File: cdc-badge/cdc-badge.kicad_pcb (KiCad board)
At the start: 4 copper layers, 85 x 110 mm, 158 parts, among them J1 USB_C, J2 JST S2B-PH-SM4-TB, J3 Conn_02x20_Odd_Even, J4 Conn_Grove, J5 Conn_02x03_Odd_Even, J6 Conn_01x06, J7 Conn_01x24, Q1 Si1308EDL, Q2 Si1308EDL, SW0 0, SW1 1, SW10 YES, SW11 NO, SW12 power on/reset, SW13 reset, SW14 flash/power off, SW15 MST-22D18G2 3J, SW16 MST-22D18G2 3J, SW2 2, SW3 3, SW4 4, SW5 5, SW6 6, SW7 7, SW8 8, SW9 9, U1 ESP32-S3-WROOM-1-N16R8, U2 TCA9535PWR, U3 TR01-C2P-T301, U5 TLV61070ADBVR, U6 BQ25895RTW, U8 TLV62569DBV

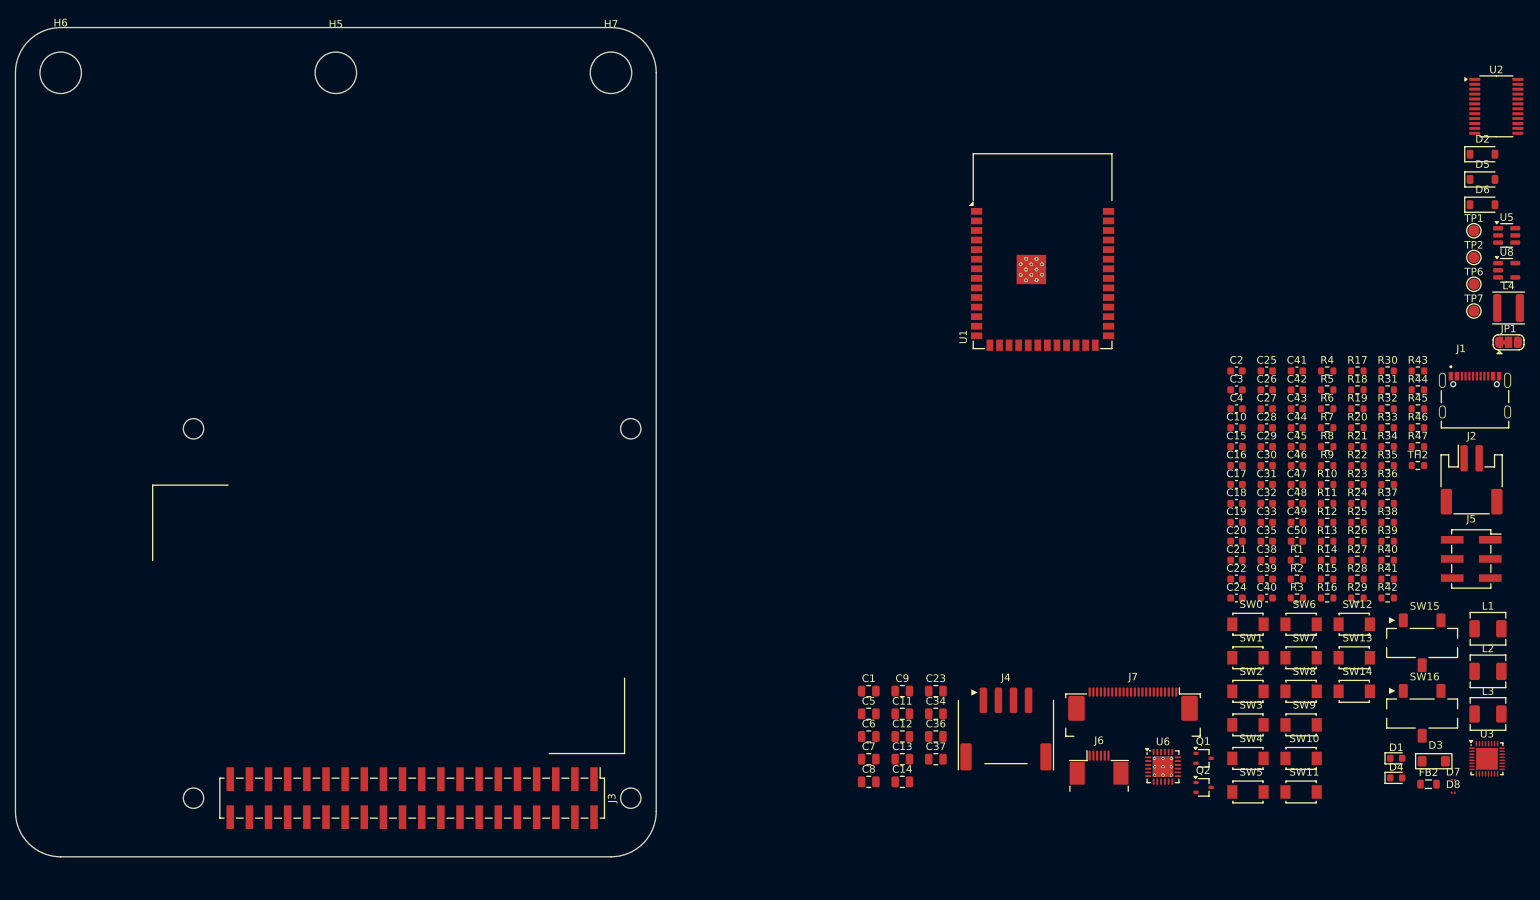
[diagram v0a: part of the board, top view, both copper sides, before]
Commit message: PCB: Placing the connectors, display and battery and lock them
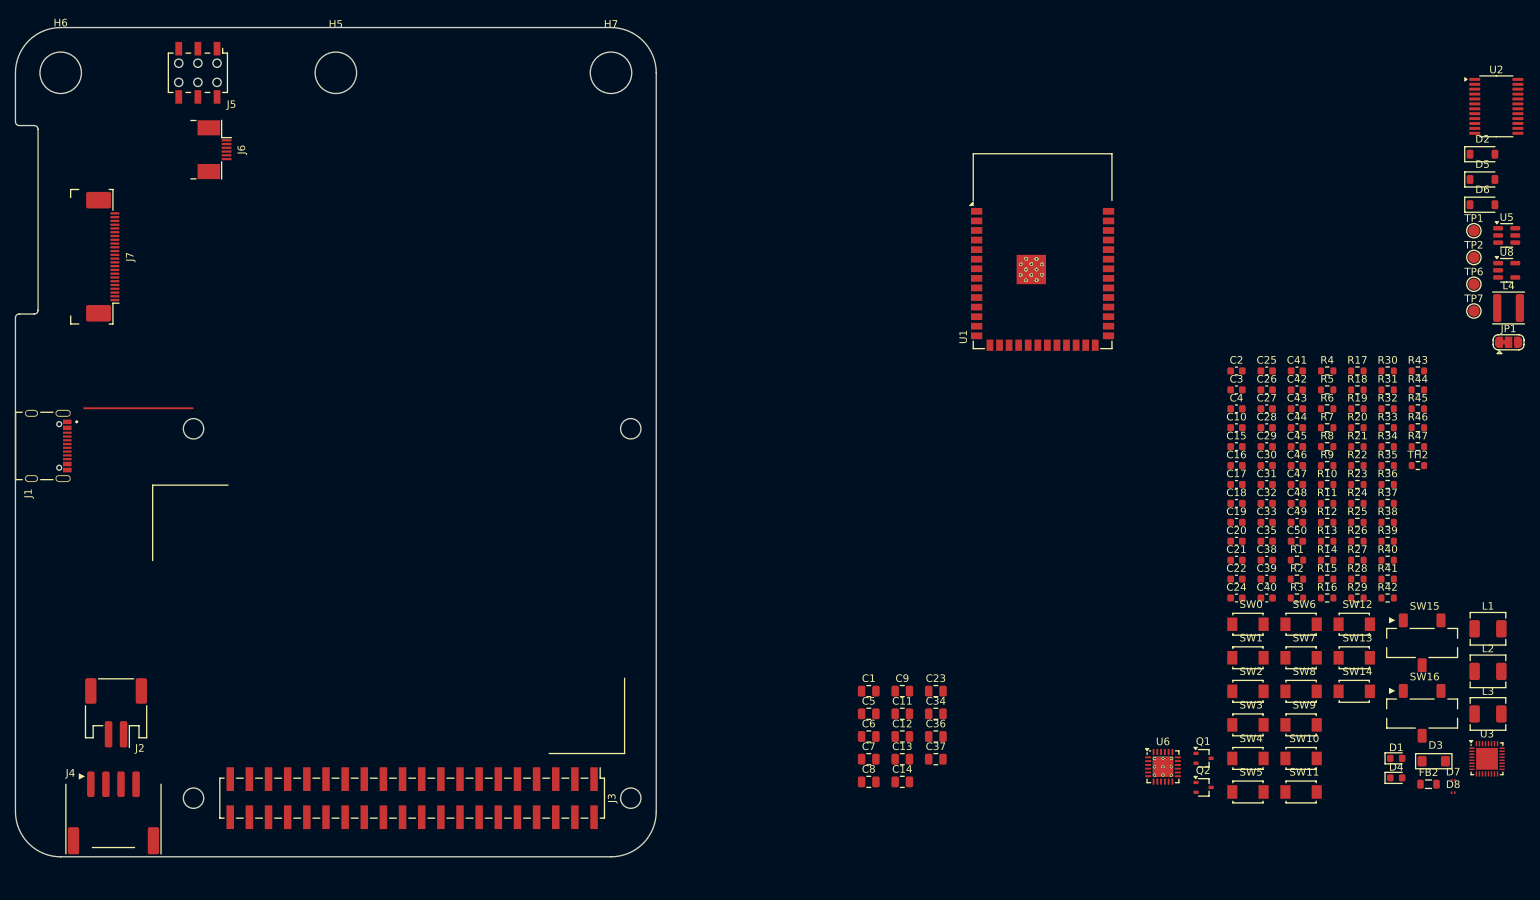
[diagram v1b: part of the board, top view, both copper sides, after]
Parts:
- J5: footprint Connector_PinSocket_2.54mm:PinSocket_2x03_P2.54mm_Vertical_SMD -> Connector_Wuerth:Wuerth_WR-PHD_610006243021_SMD_2x03_P2.54mm_Vertical
- moved J1 190.5 mm to (58.2, 104.5), turned to -90 degrees
- moved J2 182.4 mm to (68.3, 139.9), turned to 180 degrees
- moved J5 180.8 mm to (79.2, 55.0), turned to -90 degrees
- moved J7 149.8 mm to (66.0, 79.4), turned to -90 degrees
- moved J6 143.1 mm to (81.4, 65.2), turned to -90 degrees
- moved J4 118.9 mm to (68.0, 154.0)
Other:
- outline, holes or cut-outs redrawn

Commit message: PCB: Sort the components to their corresponding role/areas
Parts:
- moved D8 216.4 mm to (44.8, 70.0)
- moved D7 214.6 mm to (45.0, 73.0)
- moved FB2 209.0 mm to (44.9, 81.0)
- moved D3 206.4 mm to (44.5, 90.0)
- moved R1 180.8 mm to (45.0, 103.0)
- moved R2 180.6 mm to (44.8, 110.0)
- moved Q1 133.7 mm to (275.0, 27.6)
- moved C34 128.8 mm to (253.0, 36.0)
- moved D4 127.7 mm to (169.2, 41.0)
- moved C23 117.8 mm to (236.1, 35.0)
- moved Q2 109.3 mm to (240.0, 44.0)
- moved L1 100.2 mm to (162.8, 80.0)
- moved JP1 100.1 mm to (182.7, 162.0)
- moved C24 98.6 mm to (260.0, 36.0)
- moved D1 95.7 mm to (162.8, 87.0)
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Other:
- board text added: "3V"
- board text added: "5V"
- board text added: "Btn"
- board text added: "Charger"
- board text added: "Epaper"
- board text added: "Expander"
- board text added: "TR"

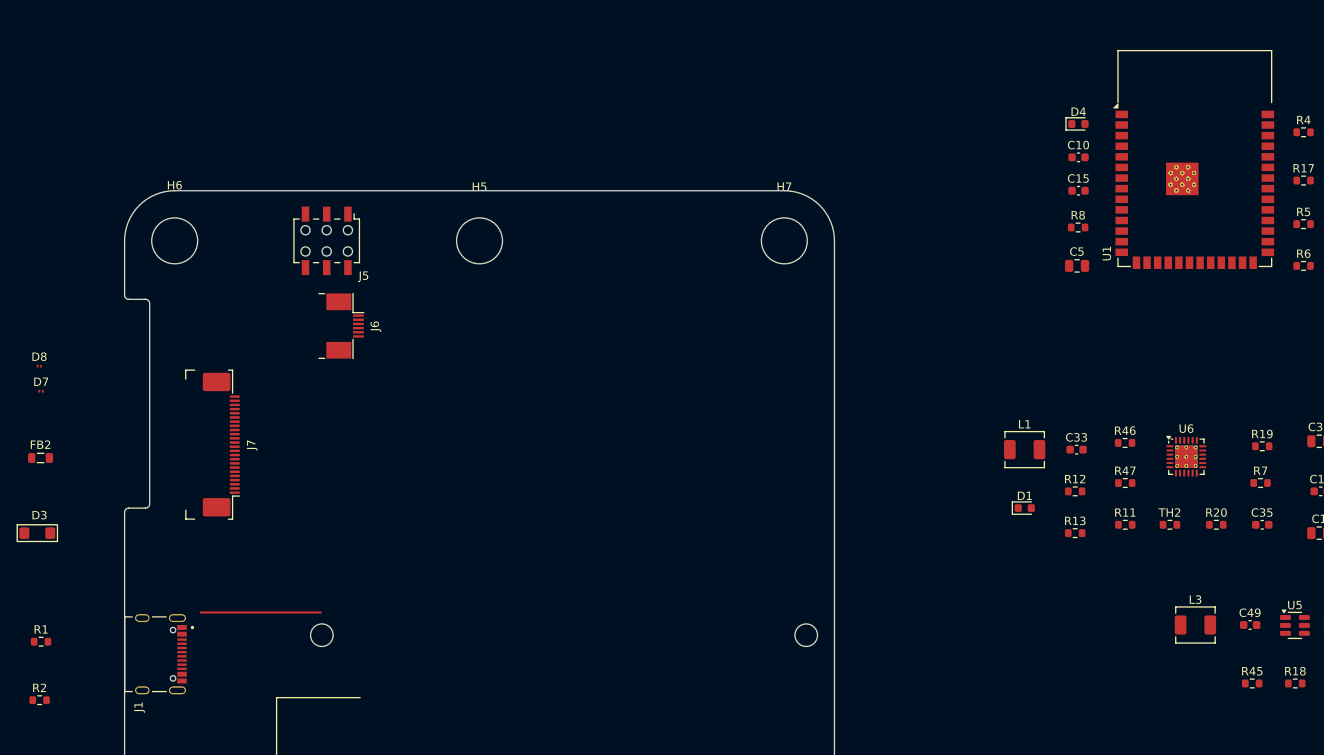
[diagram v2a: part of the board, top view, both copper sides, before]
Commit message: PCB: USB-C, Datatracks and Charging IC placement draft
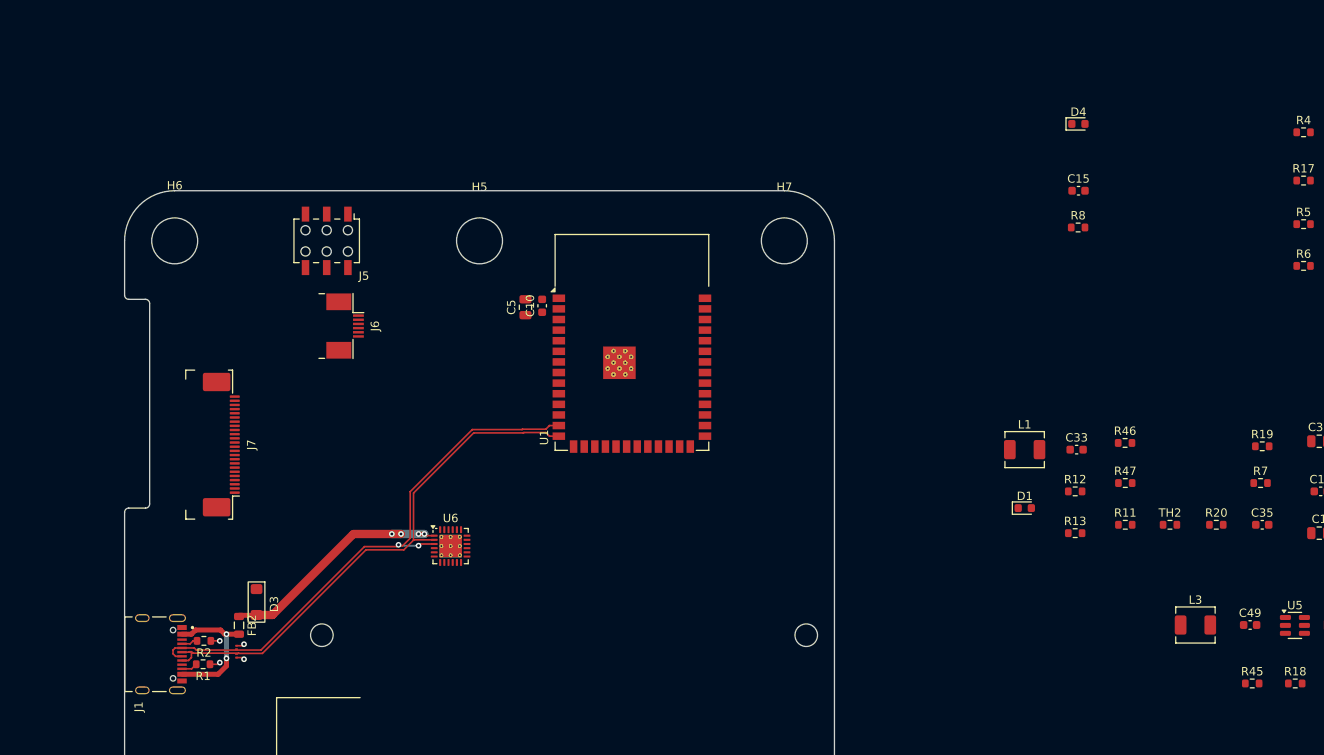
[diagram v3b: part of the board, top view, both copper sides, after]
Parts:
- moved U6 88.7 mm to (94.0, 91.5)
- moved U1 70.9 mm to (115.8, 67.1)
- moved C10 66.6 mm to (105.0, 62.8), turned to 90 degrees
- moved C5 66.2 mm to (103.0, 63.0), turned to 90 degrees
- moved D8 42.0 mm to (68.4, 104.7), turned to -90 degrees
- moved D7 38.6 mm to (68.4, 103.7), turned to 90 degrees
- moved FB2 31.1 mm to (68.7, 101.0), turned to -90 degrees
- moved D3 27.5 mm to (70.8, 98.2), turned to -90 degrees
- moved R2 20.9 mm to (64.5, 102.9), turned to 180 degrees
- moved R1 19.6 mm to (64.4, 105.7), turned to 180 degrees
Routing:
- net /USB_D-: track 0.00 -> 66.9 mm, vias 0 -> 2
- net /USB_D+: track 0.00 -> 64.1 mm
- net VBUS: track 0.00 -> 29.1 mm, vias 0 -> 4
- net /PRE_VBUS: track 0.00 -> 16.8 mm, vias 0 -> 2
- net GND: track 0.00 -> 4.29 mm, vias 0 -> 4
- net Net-(J1-CC1): track 0.00 -> 1.94 mm
- net Net-(J1-CC2): track 0.00 -> 1.93 mm

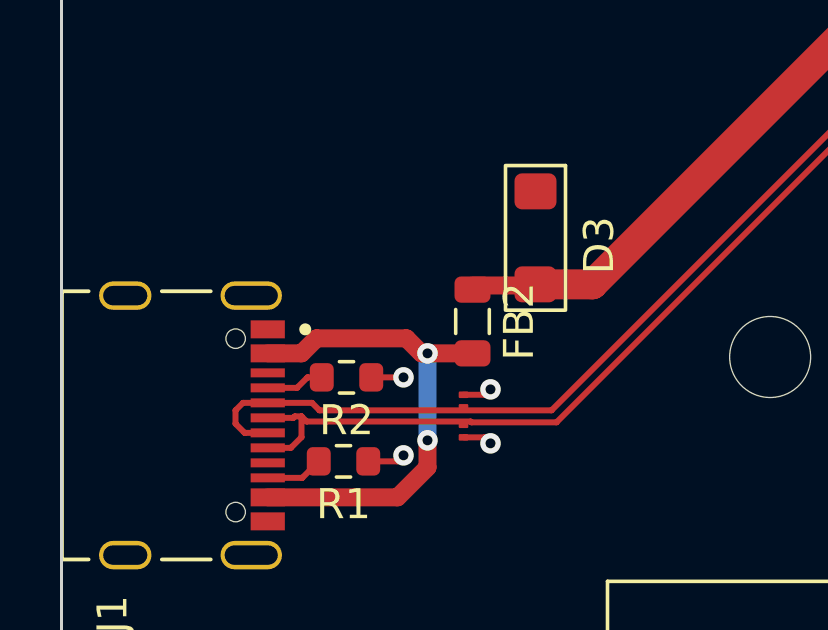
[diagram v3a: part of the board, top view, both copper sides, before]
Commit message: pcb: set default widths and clearances, try copper pours
Defaults set for both tracks and vias.
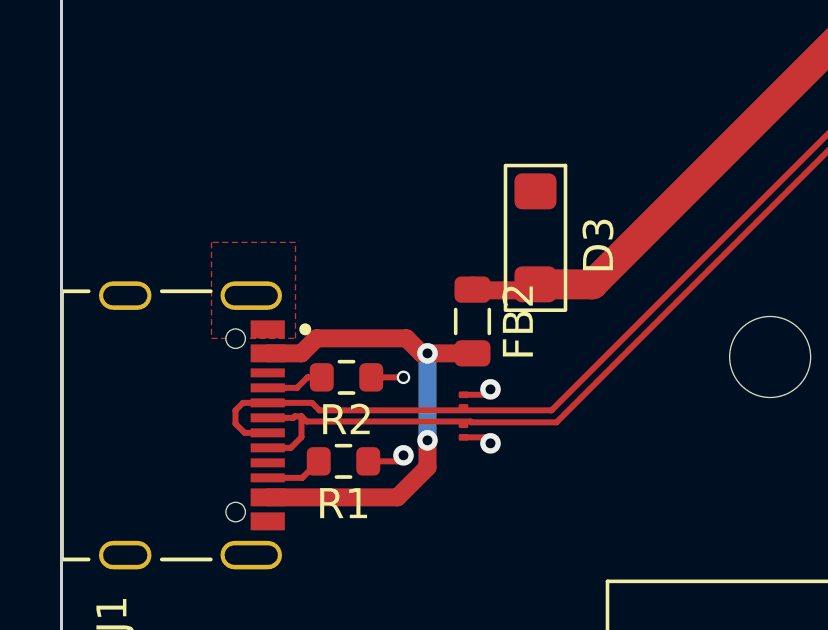
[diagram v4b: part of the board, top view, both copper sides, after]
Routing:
- added copper zone on F.Cu, net GND
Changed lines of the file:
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@@
 		(0 "F.Cu" signal)
 		(4 "In1.Cu" power "In1.Cu.GND")
-		(6 "In2.Cu" power "In2.Cu.VCC")
+		(6 "In2.Cu" power "In2.Cu.GND")
 		(2 "B.Cu" signal)
 		(9 "F.Adhes" user "F.Adhesive")
@@
 	)
 	(via
-		(at 69.3 105.1)
-		(size 0.6858)
-		(drill 0.3302)
+		(at 66.4 102.9)
+		(size 0.45)
+		(drill 0.3)
 		(layers "F.Cu" "B.Cu")
 		(net 1)
 	)
 	(via
-		(at 66.4 105.5)
+		(at 69.3 105.1)
 		(size 0.6858)
 		(drill 0.3302)
@@
 	)
 	(via
-		(at 66.4 102.9)
+		(at 66.4 105.5)
 		(size 0.6858)
 		(drill 0.3302)
@@
 	)
 	(segment
-		(start 70.7625 99.8375)
-		(end 70.8 99.8)
-		(width 0.6)
-		(layer "F.Cu")
-		(net 55)
-	)
-	(segment
-		(start 68.7 99.8375)
-		(end 70.7625 99.8375)
-		(width 0.6)
-		(layer "F.Cu")
-		(net 55)
-	)
-	(segment
 		(start 72.7 99.8)
 		(end 82.3 90.2)
@@
 	)
 	(segment
+		(start 70.6 100)
+		(end 70.8 99.8)
+		(width 0.6)
+		(layer "F.Cu")
+		(net 55)
+	)
+	(segment
 		(start 91.1 90.3)
 		(end 90.9 90.1)
@@
 		(net 55)
 	)
+	(segment
+		(start 68.8625 100)
+		(end 70.6 100)
+		(width 0.6)
+		(layer "F.Cu")
+		(net 55)
+	)
+	(segment
+		(start 68.7 99.8375)
+		(end 68.8625 100)
+		(width 0.6)
+		(layer "F.Cu")
+		(net 55)
+	)
 	(via
 		(at 87 90.1)
@@
 		(net 75)
 	)
+	(zone
+		(net 1)
+		(net_name "GND")
+		(layer "F.Cu")
+		(hatch edge 0.5)
+		(connect_pads yes
+			(clearance 0.2)
+		)
+		(min_thickness 0.2)
+		(filled_areas_thickness no)
+		(fill yes
+			(thermal_gap 0.5)
+			(thermal_bridge_width 0.5)
+		)
+		(polygon
+			(pts
+				(xy 60 101.6) (xy 62.8 101.6) (xy 62.8 98.4) (xy 60 98.4)
+			)
+		)
+	)
 	(embedded_fonts no)

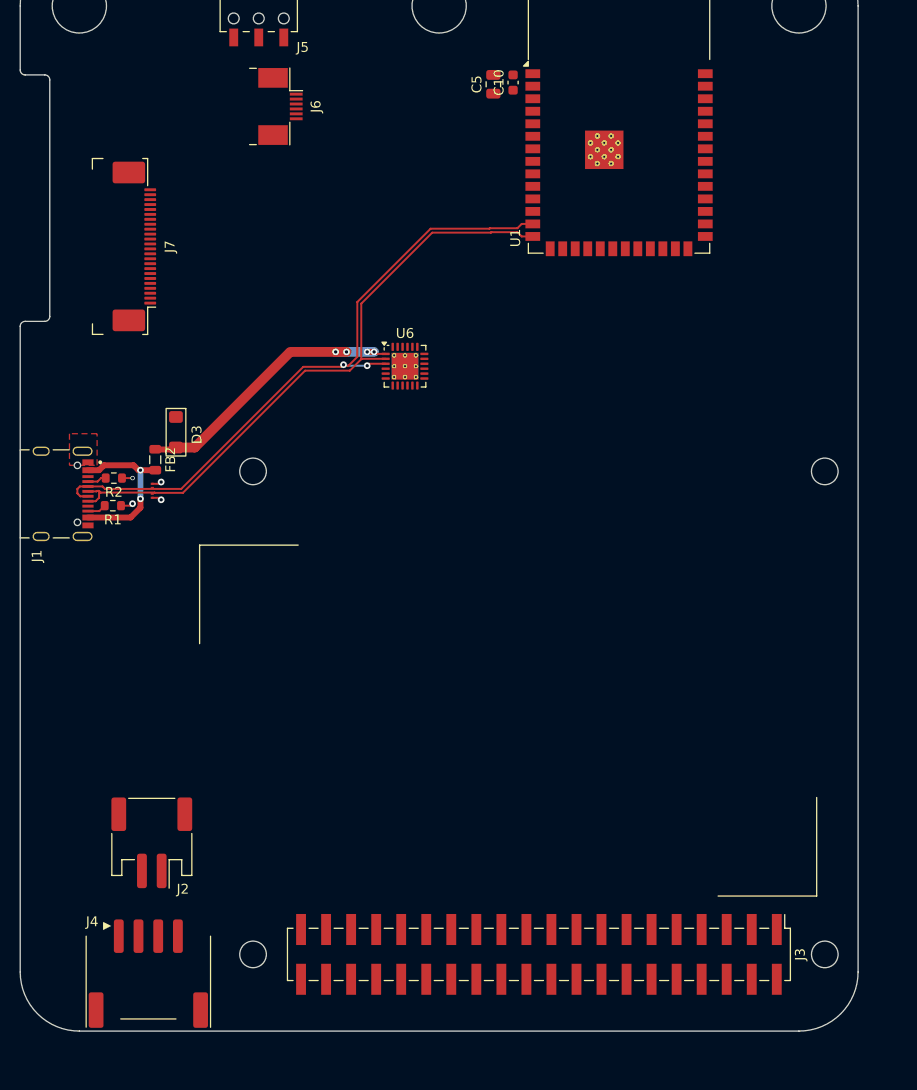
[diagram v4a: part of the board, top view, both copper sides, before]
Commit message: PCB: 3V3 area pour on front and back, GND pour on inner layers. Area prio adjust
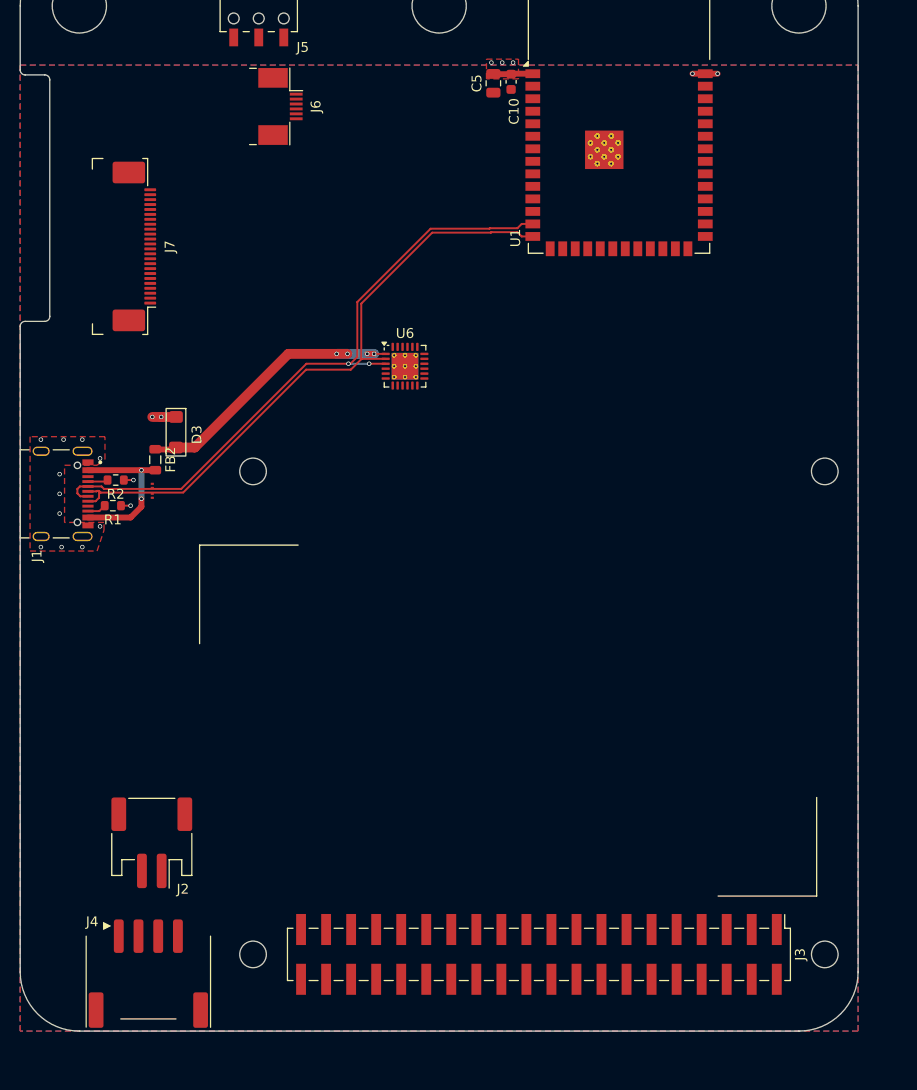
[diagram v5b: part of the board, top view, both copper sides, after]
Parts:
- moved R2 0.27 mm to (64.7, 103.1)
- moved C10 0.21 mm to (104.8, 62.7)
- moved C5 0.10 mm to (103.0, 62.9)
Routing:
- net GND: track 4.29 -> 10.8 mm, vias 4 -> 20
- net /USB_D-: track 66.9 -> 66.2 mm
- added copper zone on B.Cu, net +3.3V
- added copper zone on F.Cu, net +3.3V
- added copper zone on In1.Cu, net GND
- added copper zone on In2.Cu, net GND
